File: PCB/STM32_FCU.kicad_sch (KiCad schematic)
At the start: 0 parts

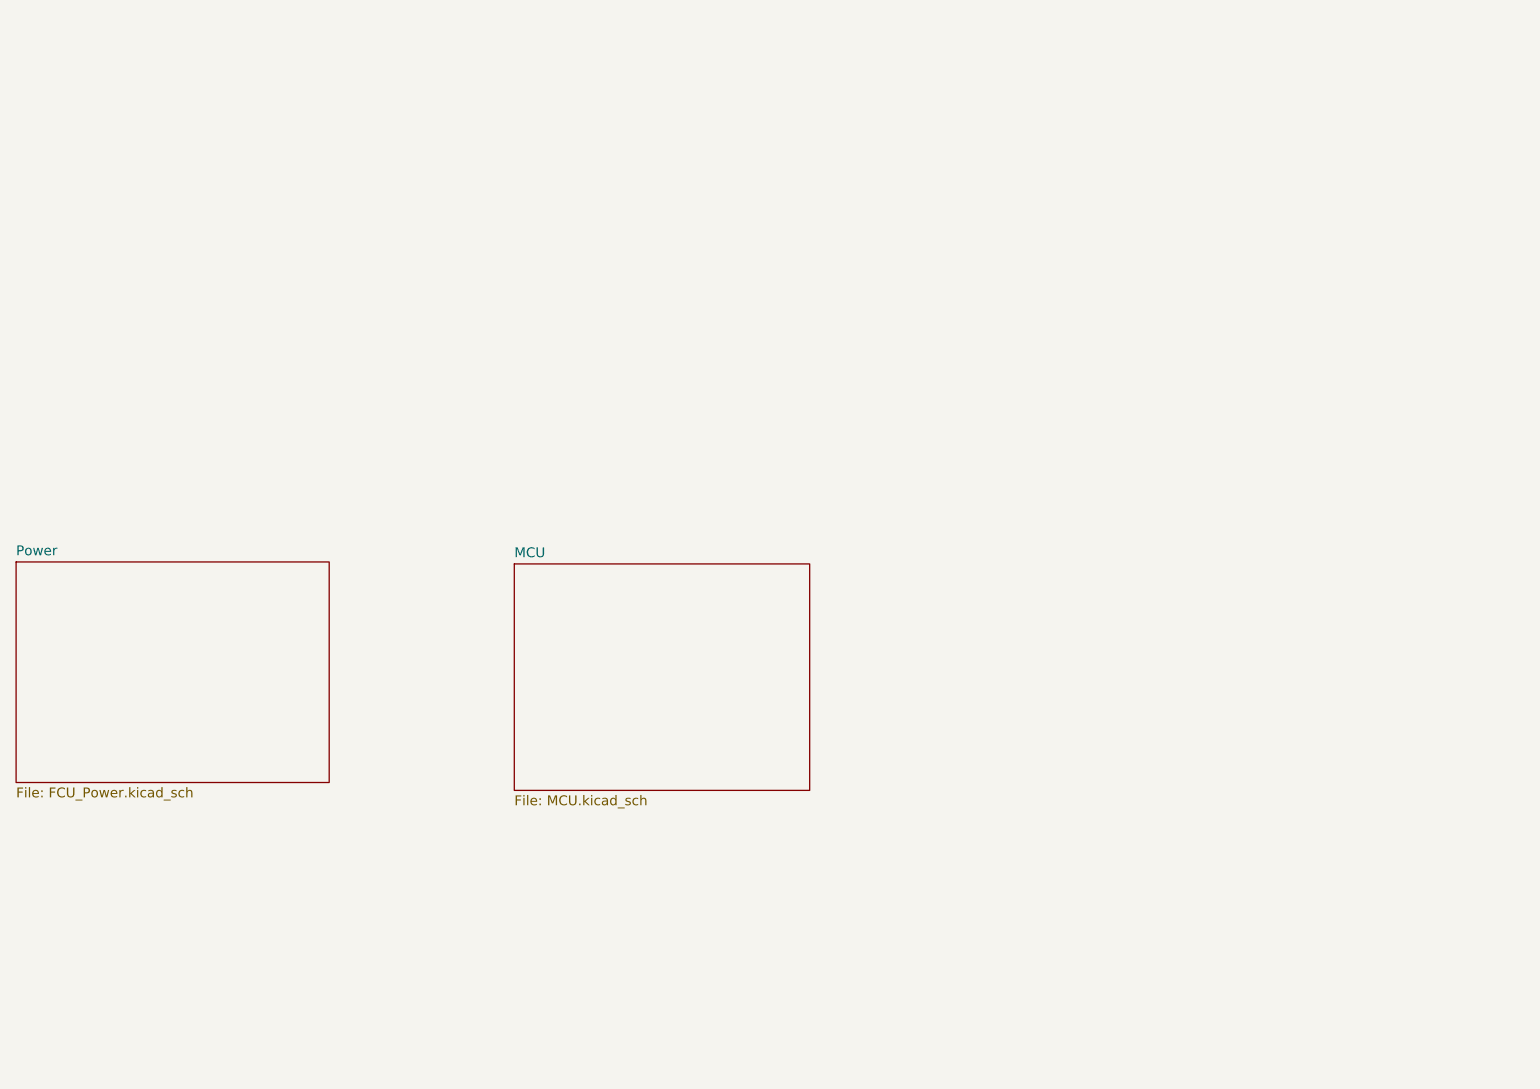
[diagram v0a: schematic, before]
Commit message: Added MCU interfaces and started sensor design
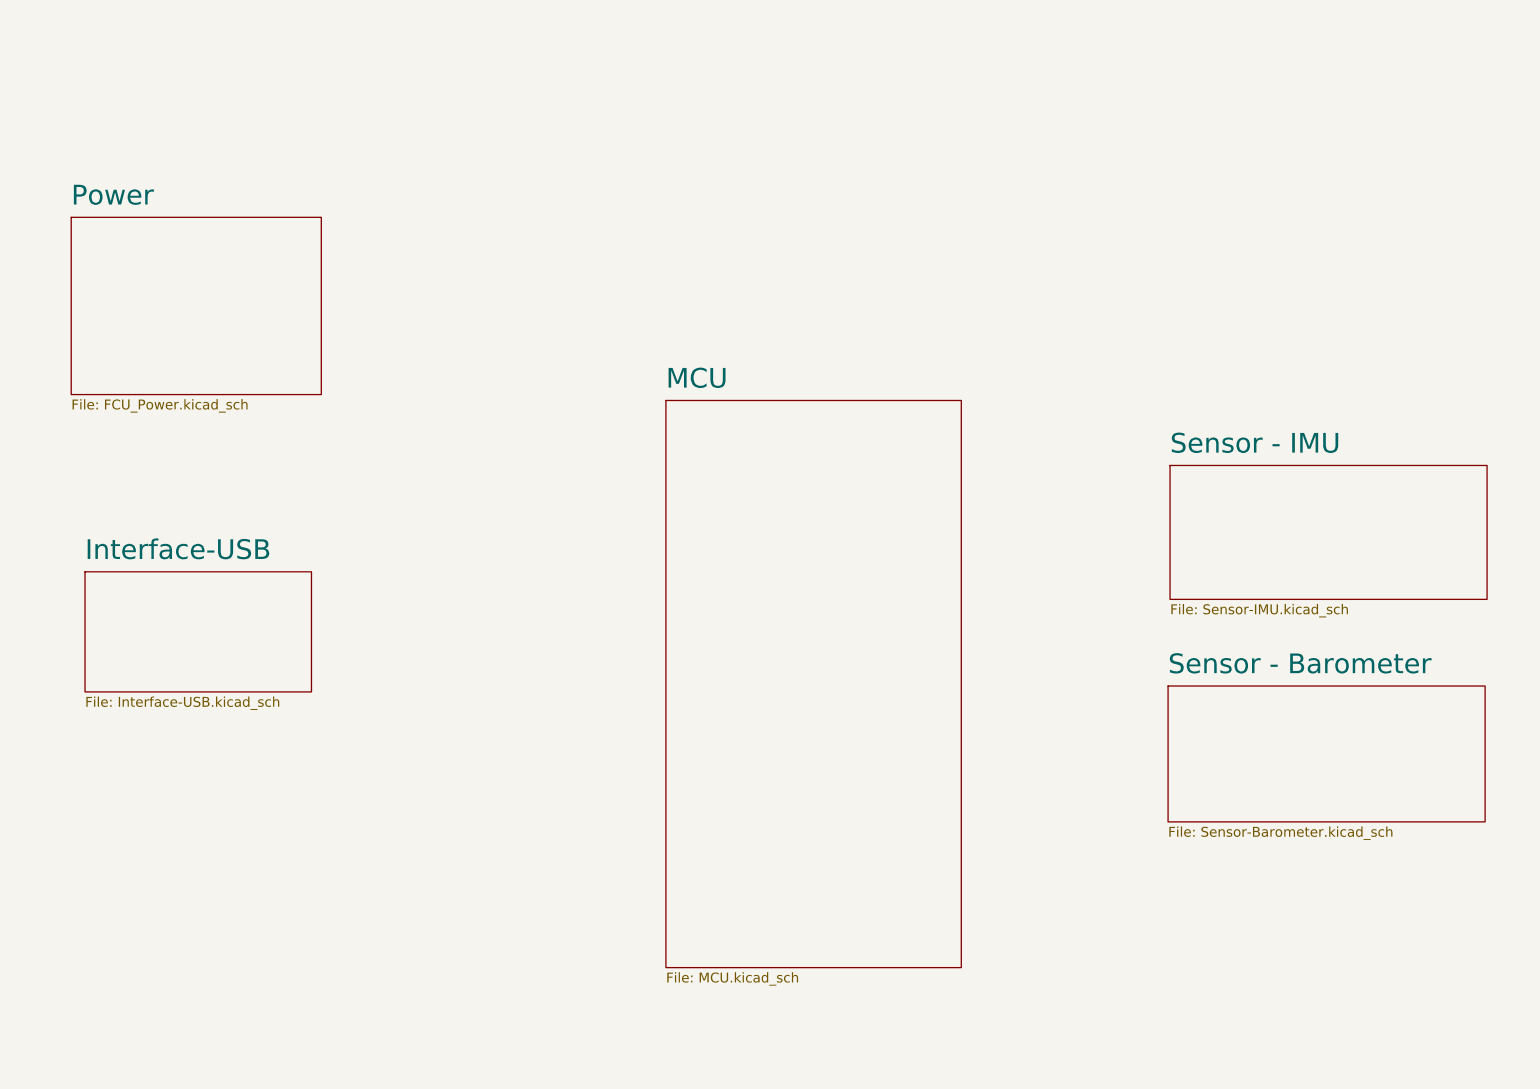
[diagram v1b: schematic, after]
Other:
- added sheet Interface-USB (Interface-USB.kicad_sch)
- added sheet Sensor - Barometer (Sensor-Barometer.kicad_sch)
- added sheet Sensor - IMU (Sensor-IMU.kicad_sch)
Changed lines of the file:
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@@
 	(paper "A")
 	(sheet
-		(at 115.57 83.82)
-		(size 38.1 29.21)
-		(exclude_from_sim no)
-		(in_bom yes)
-		(on_board yes)
-		(dnp no)
-		(fields_autoplaced yes)
-		(stroke
-			(width 0.1524)
-			(type solid)
-		)
-		(fill
-			(color 0 0 0 0)
+		(at 200.152 71.12)
+		(size 40.894 17.272)
+		(exclude_from_sim no)
+		(in_bom yes)
+		(on_board yes)
+		(dnp no)
+		(fields_autoplaced yes)
+		(stroke
+			(width 0.1524)
+			(type solid)
+		)
+		(fill
+			(color 0 194 0 0.5019607843)
+		)
+		(property "Sheetname" "Sensor - IMU"
+			(at 200.152 69.7734 0)
+			(show_name no)
+			(do_not_autoplace no)
+			(effects
+				(font
+					(size 2.54 2.54)
+				)
+				(justify left bottom)
+			)
+		)
+		(property "Sheetfile" "Sensor-IMU.kicad_sch"
+			(at 200.152 88.9766 0)
+			(show_name no)
+			(do_not_autoplace no)
+			(effects
+				(font
+					(size 1.27 1.27)
+				)
+				(justify left top)
+			)
+		)
+		(instances
+			(project "STM32_FCU"
+				(path "/9fd53907-6a99-448d-8671-d17de9d6fa45"
+					(page "5")
+				)
+			)
+		)
+	)
+	(sheet
+		(at 135.128 62.738)
+		(size 38.1 73.152)
+		(exclude_from_sim no)
+		(in_bom yes)
+		(on_board yes)
+		(dnp no)
+		(fields_autoplaced yes)
+		(stroke
+			(width 0.1524)
+			(type solid)
+		)
+		(fill
+			(color 0 132 132 0.5019607843)
 		)
 		(property "Sheetname" "MCU"
-			(at 115.57 83.1084 0)
-			(show_name no)
-			(do_not_autoplace no)
-			(effects
-				(font
-					(size 1.27 1.27)
+			(at 135.128 61.3914 0)
+			(show_name no)
+			(do_not_autoplace no)
+			(effects
+				(font
+					(size 2.54 2.54)
 				)
 				(justify left bottom)
@@
 		)
 		(property "Sheetfile" "MCU.kicad_sch"
-			(at 115.57 113.6146 0)
+			(at 135.128 136.4746 0)
 			(show_name no)
 			(do_not_autoplace no)
@@
 	)
 	(sheet
-		(at 51.308 83.566)
-		(size 40.386 28.448)
-		(exclude_from_sim no)
-		(in_bom yes)
-		(on_board yes)
-		(dnp no)
-		(fields_autoplaced yes)
-		(stroke
-			(width 0.1524)
-			(type solid)
-		)
-		(fill
-			(color 0 0 0 0)
+		(at 58.42 39.116)
+		(size 32.258 22.86)
+		(exclude_from_sim no)
+		(in_bom yes)
+		(on_board yes)
+		(dnp no)
+		(fields_autoplaced yes)
+		(stroke
+			(width 0.1524)
+			(type solid)
+		)
+		(fill
+			(color 255 229 191 0.5019607843)
 		)
 		(property "Sheetname" "Power"
-			(at 51.308 82.8544 0)
-			(show_name no)
-			(do_not_autoplace no)
-			(effects
-				(font
-					(size 1.27 1.27)
+			(at 58.42 37.7694 0)
+			(show_name no)
+			(do_not_autoplace no)
+			(effects
+				(font
+					(size 2.54 2.54)
 				)
 				(justify left bottom)
@@
 		)
 		(property "Sheetfile" "FCU_Power.kicad_sch"
-			(at 51.308 112.5986 0)
+			(at 58.42 62.5606 0)
 			(show_name no)
 			(do_not_autoplace no)
@@
 				)
 			)
+		)
+	)
+	(sheet
+		(at 60.198 84.836)
+		(size 29.21 15.494)
+		(exclude_from_sim no)
+		(in_bom yes)
+		(on_board yes)
+		(dnp no)
+		(fields_autoplaced yes)
+		(stroke
+			(width 0.1524)
+			(type solid)
+		)
+		(fill
+			(color 132 0 132 0.5019607843)
+		)
+		(property "Sheetname" "Interface-USB"
+			(at 60.198 83.4894 0)
+			(show_name no)
+			(do_not_autoplace no)
+			(effects
+				(font
+					(size 2.54 2.54)
+				)
+				(justify left bottom)
+			)
+		)
+		(property "Sheetfile" "Interface-USB.kicad_sch"
+			(at 60.198 100.9146 0)
+			(show_name no)
+			(do_not_autoplace no)
+			(effects
+				(font
+					(size 1.27 1.27)
+				)
+				(justify left top)
+			)
+		)
+		(instances
+			(project "STM32_FCU"
+				(path "/9fd53907-6a99-448d-8671-d17de9d6fa45"
+					(page "4")
+				)
+			)
+		)
+	)
+	(sheet
+		(at 199.898 99.568)
+		(size 40.894 17.526)
+		(exclude_from_sim no)
+		(in_bom yes)
+		(on_board yes)
+		(dnp no)
+		(fields_autoplaced yes)
+		(stroke
+			(width 0.1524)
+			(type solid)
+		)
+		(fill
+			(color 0 194 0 0.5019607843)
+		)
+		(property "Sheetname" "Sensor - Barometer"
+			(at 199.898 98.2214 0)
+			(show_name no)
+			(do_not_autoplace no)
+			(effects
+				(font
+					(size 2.54 2.54)
+				)
+				(justify left bottom)
+			)
+		)
+		(property "Sheetfile" "Sensor-Barometer.kicad_sch"
+			(at 199.898 117.6786 0)
+			(show_name no)
+			(do_not_autoplace no)
+			(effects
+				(font
+					(size 1.27 1.27)
+				)
+				(justify left top)
+			)
+		)
+		(instances
+			(project "STM32_FCU"
+				(path "/9fd53907-6a99-448d-8671-d17de9d6fa45"
+					(page "6")
+				)
+			)

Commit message: Added Barometer and Started External Sensors
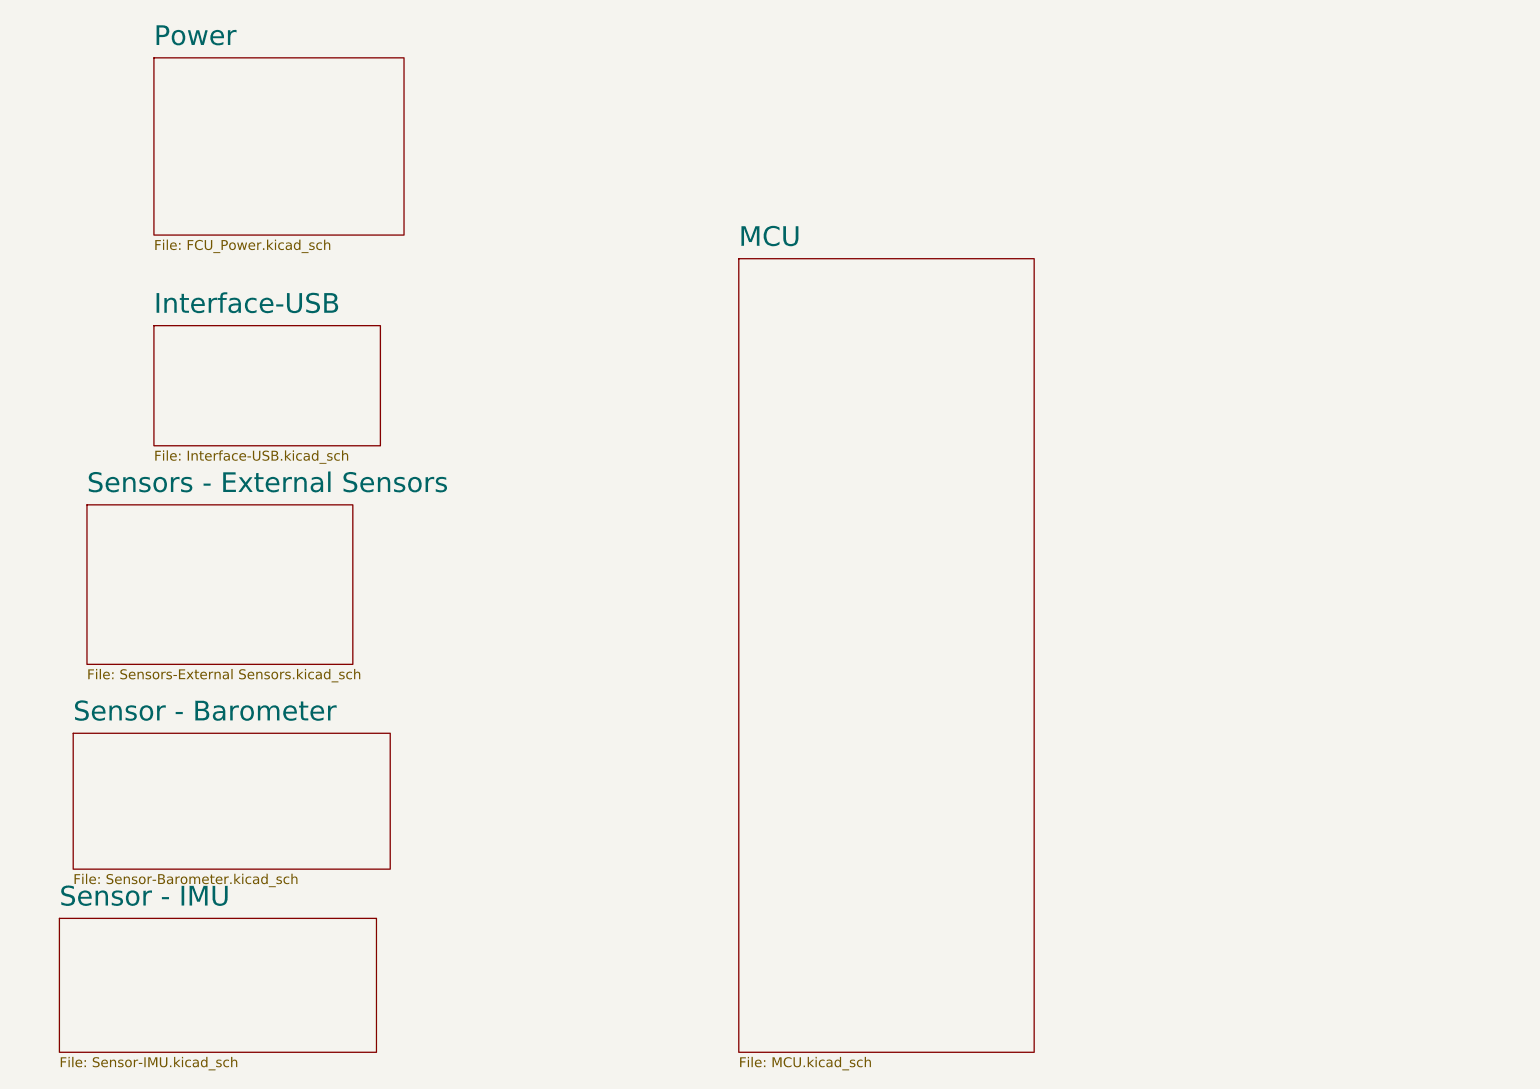
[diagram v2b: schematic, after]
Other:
- added sheet Sensors - External Sensors (Sensors-External Sensors.kicad_sch)
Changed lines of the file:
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@@
 	(paper "A")
 	(sheet
-		(at 200.152 71.12)
+		(at 60.452 76.2)
+		(size 34.29 20.574)
+		(exclude_from_sim no)
+		(in_bom yes)
+		(on_board yes)
+		(dnp no)
+		(fields_autoplaced yes)
+		(stroke
+			(width 0.1524)
+			(type solid)
+		)
+		(fill
+			(color 0 194 0 0.5019607843)
+		)
+		(property "Sheetname" "Sensors - External Sensors"
+			(at 60.452 74.8534 0)
+			(show_name no)
+			(do_not_autoplace no)
+			(effects
+				(font
+					(size 2.54 2.54)
+				)
+				(justify left bottom)
+			)
+		)
+		(property "Sheetfile" "Sensors-External Sensors.kicad_sch"
+			(at 60.452 97.3586 0)
+			(show_name no)
+			(do_not_autoplace no)
+			(effects
+				(font
+					(size 1.27 1.27)
+				)
+				(justify left top)
+			)
+		)
+		(instances
+			(project "STM32_FCU"
+				(path "/9fd53907-6a99-448d-8671-d17de9d6fa45"
+					(page "7")
+				)
+			)
+		)
+	)
+	(sheet
+		(at 56.896 129.54)
 		(size 40.894 17.272)
 		(exclude_from_sim no)
@@
 		)
 		(property "Sheetname" "Sensor - IMU"
-			(at 200.152 69.7734 0)
+			(at 56.896 128.1934 0)
 			(show_name no)
 			(do_not_autoplace no)
@@
 		)
 		(property "Sheetfile" "Sensor-IMU.kicad_sch"
-			(at 200.152 88.9766 0)
+			(at 56.896 147.3966 0)
 			(show_name no)
 			(do_not_autoplace no)
@@
 	)
 	(sheet
-		(at 135.128 62.738)
-		(size 38.1 73.152)
+		(at 144.526 44.45)
+		(size 38.1 102.362)
 		(exclude_from_sim no)
 		(in_bom yes)
@@
 		)
 		(property "Sheetname" "MCU"
-			(at 135.128 61.3914 0)
+			(at 144.526 43.1034 0)
 			(show_name no)
 			(do_not_autoplace no)
@@
 		)
 		(property "Sheetfile" "MCU.kicad_sch"
-			(at 135.128 136.4746 0)
+			(at 144.526 147.3966 0)
 			(show_name no)
 			(do_not_autoplace no)
@@
 	)
 	(sheet
-		(at 58.42 39.116)
+		(at 69.088 18.542)
 		(size 32.258 22.86)
 		(exclude_from_sim no)
@@
 		)
 		(property "Sheetname" "Power"
-			(at 58.42 37.7694 0)
+			(at 69.088 17.1954 0)
 			(show_name no)
 			(do_not_autoplace no)
@@
 		)
 		(property "Sheetfile" "FCU_Power.kicad_sch"
-			(at 58.42 62.5606 0)
+			(at 69.088 41.9866 0)
 			(show_name no)
 			(do_not_autoplace no)
@@
 	)
 	(sheet
-		(at 60.198 84.836)
+		(at 69.088 53.086)
 		(size 29.21 15.494)
 		(exclude_from_sim no)
@@
 		)
 		(property "Sheetname" "Interface-USB"
-			(at 60.198 83.4894 0)
+			(at 69.088 51.7394 0)
 			(show_name no)
 			(do_not_autoplace no)
@@
 		)
 		(property "Sheetfile" "Interface-USB.kicad_sch"
-			(at 60.198 100.9146 0)
+			(at 69.088 69.1646 0)
 			(show_name no)
 			(do_not_autoplace no)
@@
 	)
 	(sheet
-		(at 199.898 99.568)
+		(at 58.674 105.664)
 		(size 40.894 17.526)
 		(exclude_from_sim no)
@@
 		)
 		(property "Sheetname" "Sensor - Barometer"
-			(at 199.898 98.2214 0)
+			(at 58.674 104.3174 0)
 			(show_name no)
 			(do_not_autoplace no)
@@
 		)
 		(property "Sheetfile" "Sensor-Barometer.kicad_sch"
-			(at 199.898 117.6786 0)
-			(show_name no)
-			(do_not_autoplace no)
+			(at 58.674 123.7746 0)
+			(show_name no)
+			(do_not_autoplace no)
